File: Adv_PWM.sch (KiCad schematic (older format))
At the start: 11 parts, among them IC1 ATTINY13-P, P1 CONN_01X03, P2 CONN_01X03, SW1 Rotary_Encoder_Switch, U1 LTV-817

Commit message: INT0 changes
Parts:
- R3: footprint Resistors_THT:R_Axial_DIN0204_L3.6mm_D1.6mm_P5.08mm_Horizontal -> Resistors_THT:R_Axial_DIN0204_L3.6mm_D1.6mm_P7.62mm_Horizontal
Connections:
- net IN: now also IC1.6 (PB1(MISO/AIN1/OC0B/INT0/PCINT1)); no longer IC1.7 (PB2(SCK/ADC1/T0/PCINT2))
- net PWM: now also IC1.7 (PB2(SCK/ADC1/T0/PCINT2)); no longer IC1.6 (PB1(MISO/AIN1/OC0B/INT0/PCINT1))
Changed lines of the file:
@@
 F 0 "R3" V 6180 4450 50  0000 C CNN
 F 1 "330R" V 6100 4450 50  0000 C CNN
-F 2 "Resistors_THT:R_Axial_DIN0204_L3.6mm_D1.6mm_P5.08mm_Horizontal" V 6030 4450 50  0001 C CNN
+F 2 "Resistors_THT:R_Axial_DIN0204_L3.6mm_D1.6mm_P7.62mm_Horizontal" V 6030 4450 50  0001 C CNN
 F 3 "" H 6100 4450 50  0000 C CNN
 	1    6100 4450
@@
 	1    0    0    -1
 $EndComp
+Text Label 4800 2800 0    60   ~ 0
+PWM
 Text Label 4800 2700 0    60   ~ 0
-PWM
-Text Label 4900 2800 0    60   ~ 0
 IN
 Text Label 4250 2950 0    60   ~ 0
@@
 	4800 2700 5000 2700
 Wire Wire Line
-	5000 2800 4900 2800
+	4800 2800 5000 2800
 Wire Wire Line
 	4800 2900 5000 2900

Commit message: Compactify a little more
This includes adding a single surface mount resistor!
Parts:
- R4: footprint Resistors_THT:R_Axial_DIN0204_L3.6mm_D1.6mm_P5.08mm_Horizontal -> Resistors_SMD:R_0805_HandSoldering
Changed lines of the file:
@@
 F 0 "R4" V 4800 3400 50  0000 C CNN
 F 1 "330R" V 4900 3400 50  0000 C CNN
-F 2 "Resistors_THT:R_Axial_DIN0204_L3.6mm_D1.6mm_P5.08mm_Horizontal" V 4830 3400 50  0001 C CNN
+F 2 "Resistors_SMD:R_0805_HandSoldering" V 4830 3400 50  0001 C CNN
 F 3 "" H 4900 3400 50  0000 C CNN
 	1    4900 3400

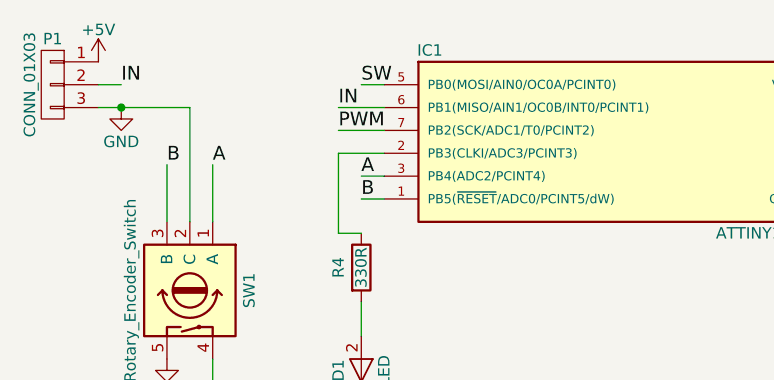
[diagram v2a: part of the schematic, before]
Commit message: Switch the PWM output to a clock pin
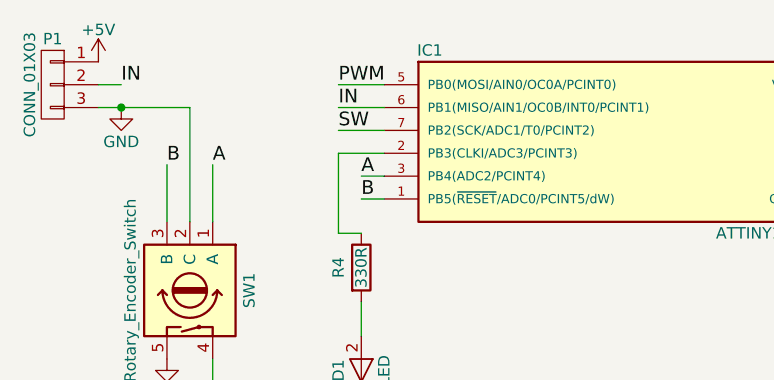
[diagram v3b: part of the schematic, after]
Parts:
- R3: footprint Resistors_THT:R_Axial_DIN0204_L3.6mm_D1.6mm_P7.62mm_Horizontal -> Resistors_THT:R_Axial_DIN0204_L3.6mm_D1.6mm_P5.08mm_Horizontal
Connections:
- net PWM: now also IC1.5 (PB0(MOSI/AIN0/OC0A/PCINT0)); no longer IC1.7 (PB2(SCK/ADC1/T0/PCINT2))
- net SW: now also IC1.7 (PB2(SCK/ADC1/T0/PCINT2)); no longer IC1.5 (PB0(MOSI/AIN0/OC0A/PCINT0))
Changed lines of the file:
@@
 F 0 "R3" V 6180 4450 50  0000 C CNN
 F 1 "330R" V 6100 4450 50  0000 C CNN
-F 2 "Resistors_THT:R_Axial_DIN0204_L3.6mm_D1.6mm_P7.62mm_Horizontal" V 6030 4450 50  0001 C CNN
+F 2 "Resistors_THT:R_Axial_DIN0204_L3.6mm_D1.6mm_P5.08mm_Horizontal" V 6030 4450 50  0001 C CNN
 F 3 "" H 6100 4450 50  0000 C CNN
 	1    6100 4450
@@
 	1    0    0    -1
 $EndComp
-Text Label 4800 2800 0    60   ~ 0
+Text Label 4800 2600 0    60   ~ 0
 PWM
 Text Label 4800 2700 0    60   ~ 0
@@
 Text Label 4900 3100 0    60   ~ 0
 B
-Text Label 4900 2600 0    60   ~ 0
+Text Label 4800 2800 0    60   ~ 0
 SW
 Text Label 5850 4200 0    60   ~ 0
@@
 	6950 4550 7550 4550
 Wire Wire Line
-	5000 2600 4900 2600
+	4800 2600 5000 2600
 Wire Wire Line
 	3850 2600 3750 2600

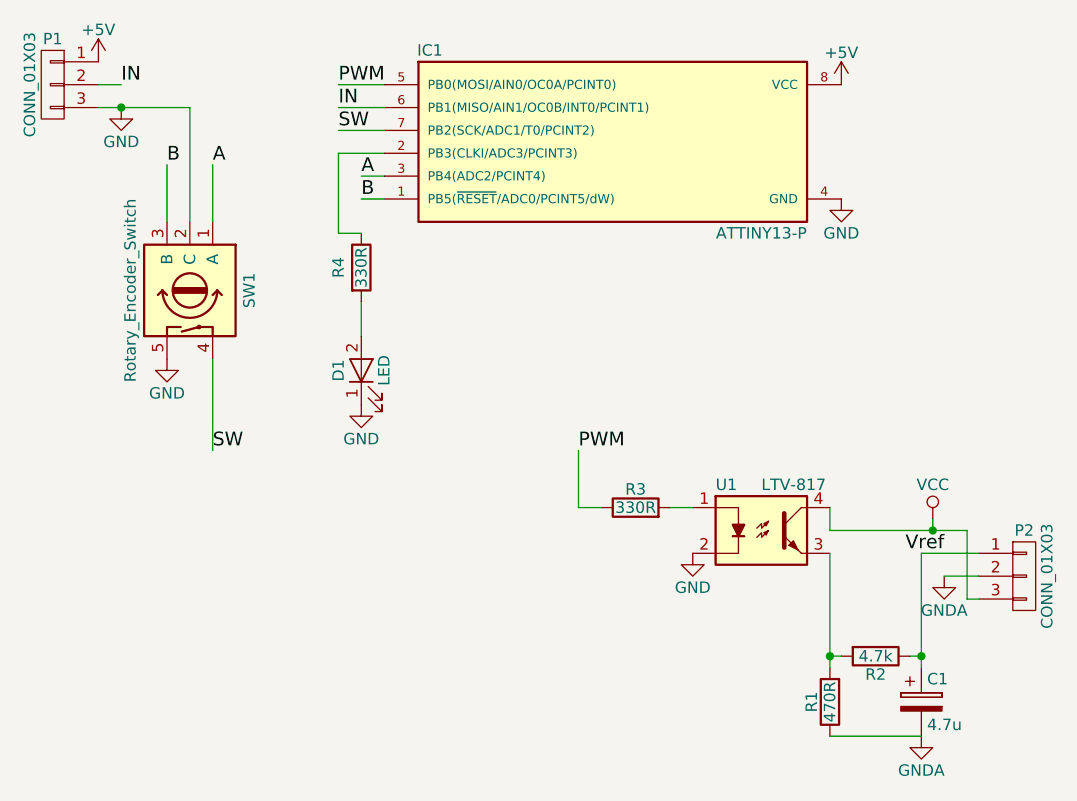
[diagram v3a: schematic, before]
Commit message: Use Voltage Divider on reset pin
this means that we no longer need the reset fuse to be set, allowing
reprogramming when testing. This required the swapping of pins and a
slightly more complicated board.
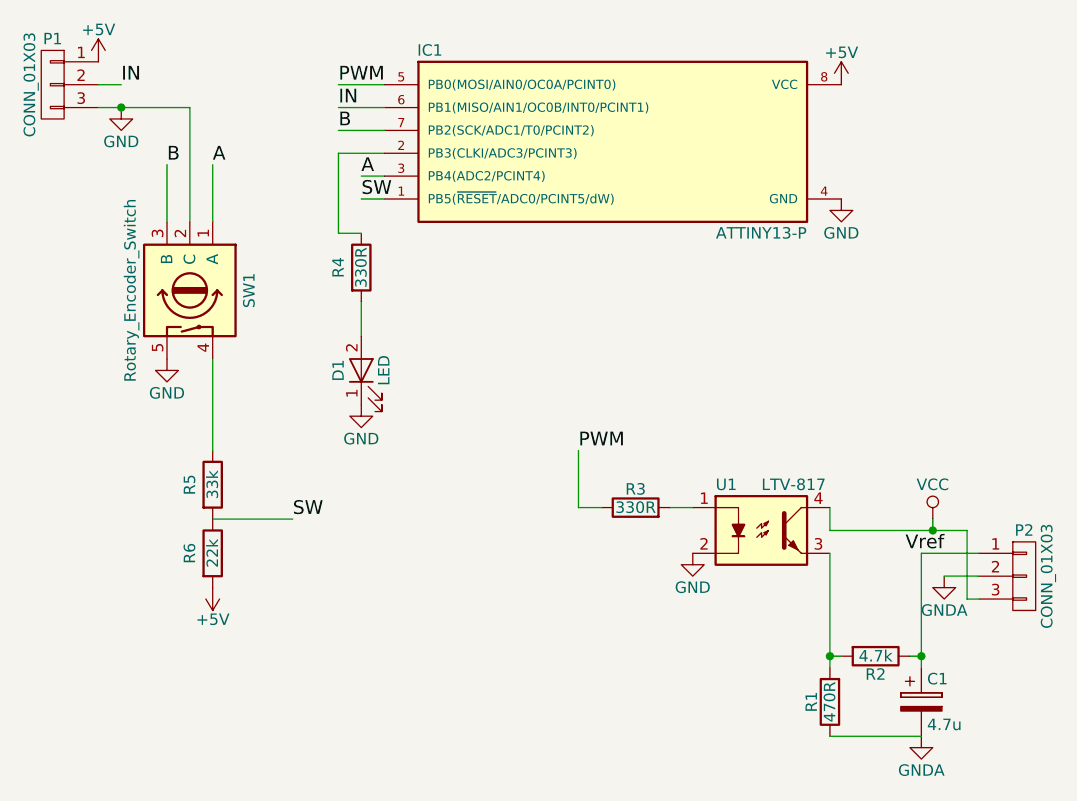
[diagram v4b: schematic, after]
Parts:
- added R5: 33k, Resistors_THT:R_Axial_DIN0204_L3.6mm_D1.6mm_P5.08mm_Horizontal, symbol R
- added R6: 22k, Resistors_THT:R_Axial_DIN0204_L3.6mm_D1.6mm_P5.08mm_Horizontal, symbol R
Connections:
- net +5V: now also R6.2
- net B: now also IC1.7 (PB2(SCK/ADC1/T0/PCINT2)); no longer IC1.1 (PB5(~RESET~/ADC0/PCINT5/dW))
- net SW: now also IC1.1 (PB5(~RESET~/ADC0/PCINT5/dW)), R5.2, R6.1; no longer IC1.7 (PB2(SCK/ADC1/T0/PCINT2)), SW1.4
- new net: R5.1, SW1.4
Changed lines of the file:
@@
 Text Label 4900 3000 0    60   ~ 0
 A
+Text Label 4800 2800 0    60   ~ 0
+B
 Text Label 4900 3100 0    60   ~ 0
-B
-Text Label 4800 2800 0    60   ~ 0
 SW
 Text Label 5850 4200 0    60   ~ 0
@@
 Wire Wire Line
 	4250 3800 4250 4200
-Text Label 4250 4200 0    60   ~ 0
+Text Label 4600 4500 0    60   ~ 0
 SW
 $Comp
@@
 Wire Wire Line
 	7550 4850 7550 4550
+$Comp
+L R R5
+U 1 1 58FB4D6E
+P 4250 4350
+F 0 "R5" V 4150 4350 50  0000 C CNN
+F 1 "33k" V 4250 4350 50  0000 C CNN
+F 2 "Resistors_THT:R_Axial_DIN0204_L3.6mm_D1.6mm_P5.08mm_Horizontal" V 4180 4350 50  0001 C CNN
+F 3 "" H 4250 4350 50  0000 C CNN
+	1    4250 4350
+	1    0    0    -1
+$EndComp
+Wire Wire Line
+	4250 4500 4600 4500
+$Comp
+L R R6
+U 1 1 58FB4E92
+P 4250 4650
+F 0 "R6" V 4150 4650 50  0000 C CNN
+F 1 "22k" V 4250 4650 50  0000 C CNN
+F 2 "Resistors_THT:R_Axial_DIN0204_L3.6mm_D1.6mm_P5.08mm_Horizontal" V 4180 4650 50  0001 C CNN
+F 3 "" H 4250 4650 50  0000 C CNN
+	1    4250 4650
+	1    0    0    -1
+$EndComp
+$Comp
+L +5V #PWR011
+U 1 1 58FB4F31
+P 4250 4800
+F 0 "#PWR011" H 4250 4650 50  0001 C CNN
+F 1 "+5V" H 4250 4940 50  0000 C CNN
+F 2 "" H 4250 4800 50  0000 C CNN
+F 3 "" H 4250 4800 50  0000 C CNN
+	1    4250 4800
+	-1   0    0    1
+$EndComp
 $EndSCHEMATC
